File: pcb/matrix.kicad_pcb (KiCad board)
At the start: 2 copper layers, 57.4 x 47.1 mm, 69 parts, among them J1 Conn_01x02, J2 USB_C_Receptacle_USB2.0_14P, SW1 SW_Push, SW2 SW_Push, SW3 SW_Push, SW4 SW_Push, U1 ESP32-S3-MINI-1U, U2 XC6206PxxxMR

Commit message: Replace components
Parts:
- removed SW4: SW_Push, Button_Switch_SMD:SW_SPST_PTS810
- added G***: LOGO, LOGO, F.Cu at (122.6, 85.0)
- added REF**: ToolingHole_1.152mm, MountingHole:ToolingHole_1.152mm, F.Cu at (116.8, 79.0)
- added REF**: ToolingHole_1.152mm, MountingHole:ToolingHole_1.152mm, F.Cu at (116.8, 122.6)
- added REF**: ToolingHole_1.152mm, MountingHole:ToolingHole_1.152mm, F.Cu at (169.6, 122.6)
- SW1, SW2, SW3: footprint Button_Switch_SMD:SW_SPST_PTS810 -> Button_Switch_SMD:SW_SPST_TS-1088-xR020
- U1: value ESP32-S3-MINI-1U -> ESP32-C3-WROOM-02; footprint RF_Module:ESP32-S2-MINI-1U -> RF_Module:ESP32-C3-WROOM-02
- moved R3 26.0 mm to (143.0, 89.8)
- moved C3 26.0 mm to (143.0, 91.5), turned to 180 degrees
- moved R4 25.0 mm to (169.8, 86.6), turned to -90 degrees
- moved SW3 8.06 mm to (130.7, 85.1)
- moved U1 3.65 mm to (158.6, 91.6)
- moved C5 2.57 mm to (143.0, 85.8)
- moved C4 2.44 mm to (143.0, 87.6)
- moved C1 1.94 mm to (156.2, 118.2)
- moved C2 1.94 mm to (148.6, 118.2)
- moved J1 1.94 mm to (164.5, 118.3)
- moved J2 1.94 mm to (164.2, 104.7)
- moved R11 1.94 mm to (154.9, 102.9)
- moved R12 1.94 mm to (154.9, 100.4)
- moved D31 1.94 mm to (152.2, 111.8)
- moved D32 1.94 mm to (152.2, 113.8)
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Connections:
- R10 pad 1: Net-(U1-IO4) -> /P6
- R11 pad 2: Net-(U1-USB_D-) -> /USB-
- R12 pad 2: Net-(U1-USB_D+) -> /USB+
- R5 pad 1: Net-(U1-IO9) -> /P1
- R6 pad 1: Net-(U1-IO8) -> /P2
- R7 pad 1: Net-(U1-IO7) -> /P3
- R8 pad 1: Net-(U1-IO6) -> /P4
- R9 pad 1: Net-(U1-IO5) -> /P5
- U1 pad 1: GND -> Net-(U1-3V3)
- U1 pad 10: Net-(U1-IO6) -> Net-(U1-IO10)
- U1 pad 11: Net-(U1-IO7) -> unconnected-(U1-IO20/RXD-Pad11)
- U1 pad 12: Net-(U1-IO8) -> unconnected-(U1-IO21/TXD-Pad12)
- U1 pad 13: Net-(U1-IO9) -> /USB-
- U1 pad 14: Net-(U1-IO10) -> /USB+
- U1 pad 15: Net-(U1-IO11) -> /P5
- U1 pad 17: unconnected-(U1-IO13-Pad17) -> /P6
- U1 pad 18: unconnected-(U1-IO14-Pad18) -> Net-(U1-IO0)
- U1 pad 19: unconnected-(U1-IO15-Pad19) -> GND
- U1 pad 2: GND -> Net-(U1-EN)
- U1 pad 3: Net-(U1-3V3) -> /P4
- U1 pad 4: Net-(U1-IO0) -> /P3
- U1 pad 5: unconnected-(U1-IO1-Pad5) -> /P2
- U1 pad 6: unconnected-(U1-IO2-Pad6) -> /P1
- U1 pad 8: Net-(U1-IO4) -> unconnected-(U1-IO9-Pad8)
- U1 pad 9: Net-(U1-IO5) -> GND
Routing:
- net /P6: track 0.00 -> 38.2 mm, vias 0 -> 2
- net /P5: track 0.00 -> 38.0 mm, vias 0 -> 2
- net Net-(U1-IO9): track 27.2 -> 0.00 mm
- net /P1: track 0.00 -> 26.7 mm
- net /P2: track 0.00 -> 25.2 mm
- net Net-(U1-IO8): track 25.0 -> 0.00 mm
- net Net-(U1-IO11): track 24.6 -> 0.00 mm, vias 2 -> 0
- net /P3: track 0.00 -> 23.7 mm
- net Net-(U1-IO7): track 23.0 -> 0.00 mm
- net Net-(U1-3V3): track 68.7 -> 91.4 mm, vias 6 -> 2
- net /P4: track 0.00 -> 22.0 mm
- net Net-(U1-EN): track 63.9 -> 42.1 mm
- net Net-(U1-IO6): track 21.2 -> 0.00 mm
- net Net-(U1-IO5): track 18.9 -> 0.00 mm
- net /USB-: track 0.00 -> 17.3 mm
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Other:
- board size 57.4 x 47.1 mm -> 56.4 x 47.1 mm

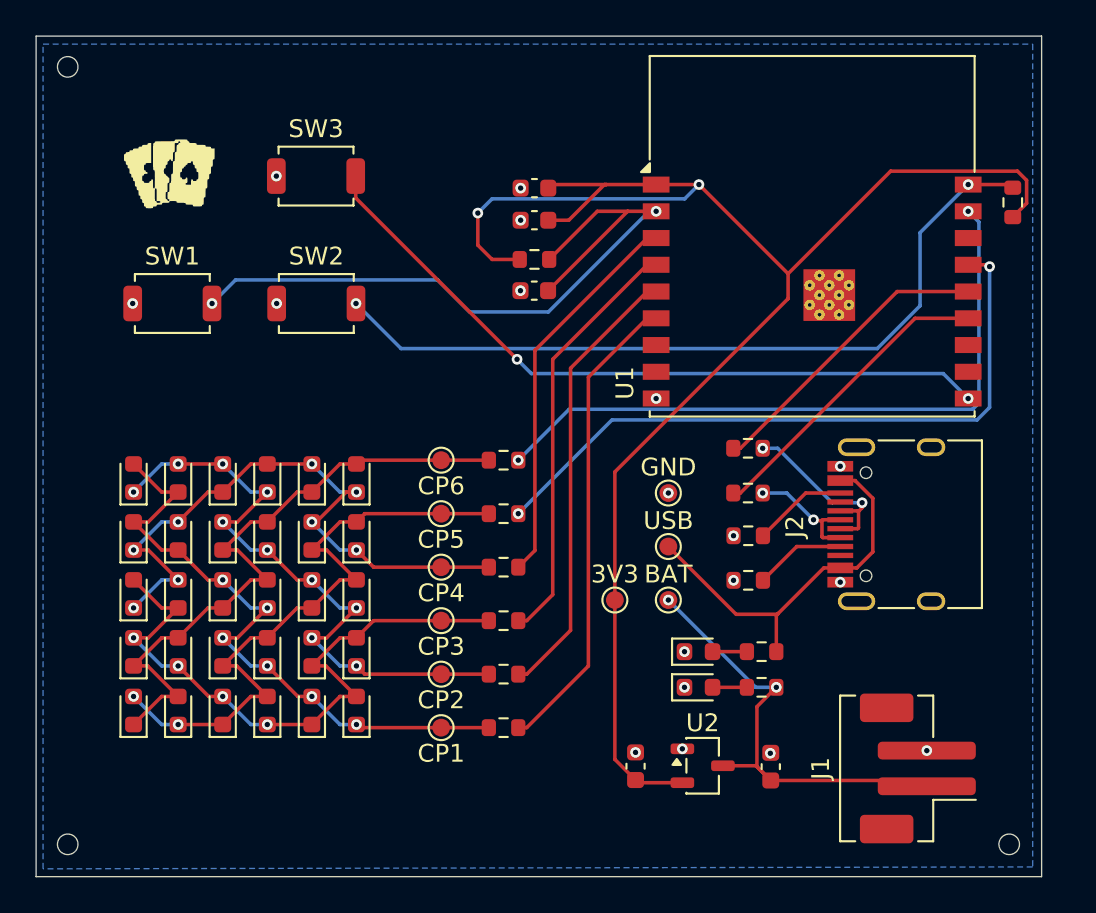
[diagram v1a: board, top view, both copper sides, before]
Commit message: Update to C6-MINI
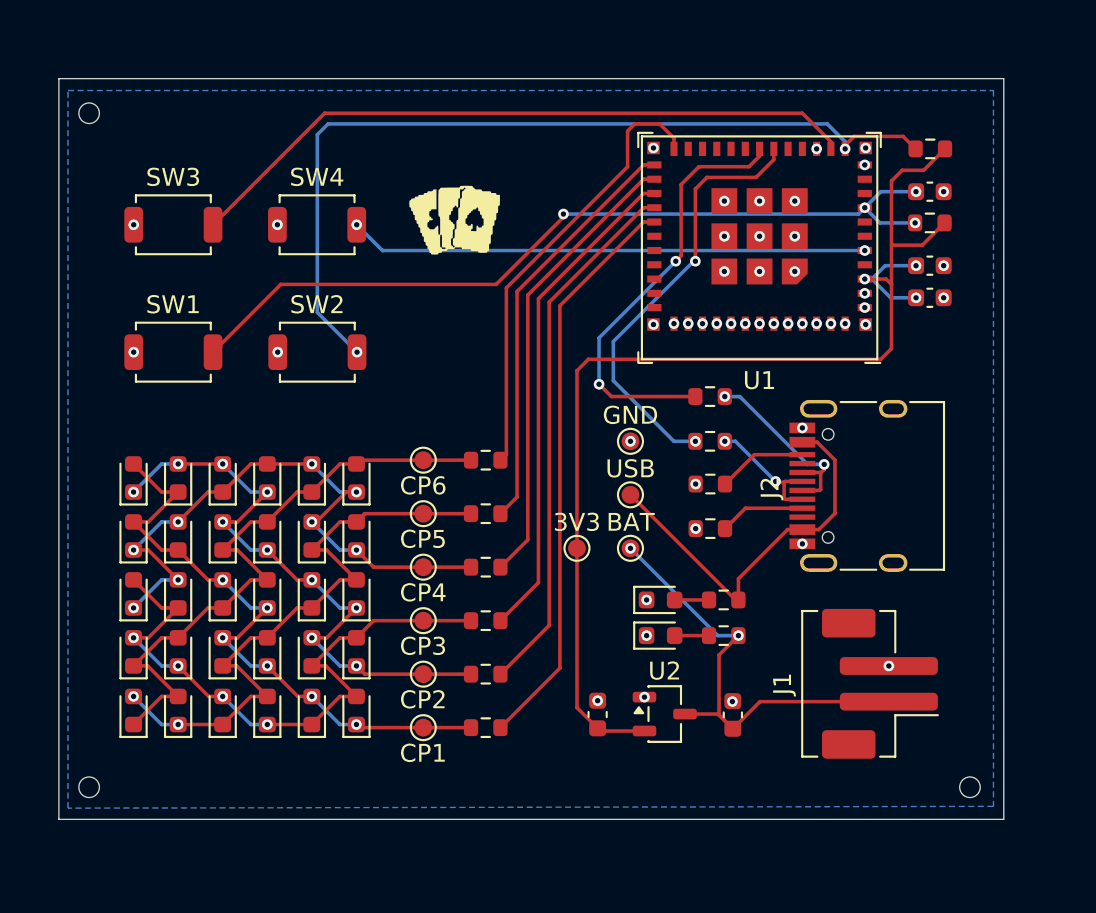
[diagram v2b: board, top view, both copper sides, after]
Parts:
- added SW4: SW_Push, Button_Switch_SMD:SW_SPST_TS-1088-xR020, F.Cu at (130.8, 87.9)
- U1: value ESP32-C3-WROOM-02 -> ESP32-C6-MINI-1/U; footprint RF_Module:ESP32-C3-WROOM-02 -> PCM_Espressif:ESP32-C6-MINI-1U
- moved C3 22.9 mm to (165.2, 86.0), turned to 0 degrees
- moved C4 22.6 mm to (165.2, 92.0)
- moved C5 22.6 mm to (165.2, 90.2)
- moved R3 22.3 mm to (165.2, 87.8), turned to 0 degrees
- moved G*** 16.2 mm to (138.6, 87.6)
- moved SW3 8.45 mm to (122.7, 87.9)
- moved R4 5.51 mm to (165.2, 83.6), turned to 0 degrees
- moved J1 5.20 mm to (162.3, 113.6)
- moved REF** 3.88 mm to (167.4, 119.4)
- moved 3V3 3.60 mm to (145.4, 106.0)
- moved BAT 3.60 mm to (148.4, 106.0)
- moved C1 3.60 mm to (154.1, 115.3)
- moved C2 3.60 mm to (146.5, 115.3)
- moved GND 3.60 mm to (148.4, 100.0)
- moved R11 3.60 mm to (152.8, 100.0)
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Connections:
- net Net-(J1-Pin_1) renamed +BATT
- 3V3 pad 1: Net-(U1-3V3) -> +3V3
- C2 pad 1: Net-(U1-3V3) -> +3V3
- C3 pad 1: Net-(U1-EN) -> /EN
- C4 pad 1: GND -> +3V3
- C4 pad 2: Net-(U1-3V3) -> GND
- C5 pad 1: GND -> +3V3
- C5 pad 2: Net-(U1-3V3) -> GND
- R11 pad 2: /USB- -> /D-
- R12 pad 2: /USB+ -> /D+
- R3 pad 1: Net-(U1-EN) -> /EN
- R3 pad 2: Net-(U1-3V3) -> +3V3
- R4 pad 1: Net-(U1-IO0) -> /GP0
- R4 pad 2: Net-(U1-3V3) -> +3V3
- SW1 pad 2: Net-(U1-EN) -> /EN
- SW2 pad 2: Net-(U1-IO0) -> /GP0
- SW3 pad 2: Net-(U1-IO10) -> /GP1
- U1 pad 1: Net-(U1-3V3) -> GND
- U1 pad 10: Net-(U1-IO10) -> unconnected-(U1-MTDI/GPIO5/ADC1_CH5-Pad10)
- U1 pad 11: unconnected-(U1-IO20/RXD-Pad11) -> GND
- U1 pad 12: unconnected-(U1-IO21/TXD-Pad12) -> /GP0
- U1 pad 13: /USB- -> /GP1
- U1 pad 14: /USB+ -> GND
- U1 pad 15: /P5 -> unconnected-(U1-MTCK/GPIO6/ADC1_CH6-Pad15)
- U1 pad 17: /P6 -> /D-
- U1 pad 18: Net-(U1-IO0) -> /D+
- U1 pad 19: GND -> unconnected-(U1-GPIO14-Pad19)
- U1 pad 2: Net-(U1-EN) -> GND
- U1 pad 3: /P4 -> +3V3
- U1 pad 4: /P3 -> unconnected-(U1-NC-Pad4)
- U1 pad 5: /P2 -> /GP2
- U1 pad 6: /P1 -> unconnected-(U1-GPIO3/ADC1_CH3-Pad6)
- U1 pad 8: unconnected-(U1-IO9-Pad8) -> /EN
- U1 pad 9: GND -> unconnected-(U1-MTMS/GPIO4/ADC1_CH4-Pad9)
- U2 pad 2: Net-(U1-3V3) -> +3V3
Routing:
- net Net-(U1-3V3): track 91.4 -> 0.00 mm, vias 2 -> 0
- net +3V3: track 0.00 -> 66.0 mm, vias 0 -> 3
- net /GP0: track 0.00 -> 48.4 mm, vias 0 -> 2
- net /EN: track 0.00 -> 46.4 mm, vias 0 -> 4
- net Net-(U1-IO0): track 44.2 -> 0.00 mm, vias 2 -> 0
- net Net-(U1-EN): track 42.1 -> 0.00 mm, vias 2 -> 0
- net Net-(U1-IO10): track 40.2 -> 0.00 mm, vias 2 -> 0
- net /GP1: track 0.00 -> 38.3 mm
- net /GP2: track 0.00 -> 29.1 mm, vias 0 -> 2
- net /D-: track 0.00 -> 24.5 mm, vias 0 -> 2
- net /D+: track 0.00 -> 24.4 mm, vias 0 -> 2
- net /USB-: track 17.3 -> 0.00 mm
- net /USB+: track 16.9 -> 0.00 mm
- net /P5: track 38.0 -> 23.5 mm, vias 2 -> 0
- net /P6: track 38.2 -> 25.1 mm, vias 2 -> 0
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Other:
- board size 56.4 x 47.1 mm -> 53 x 41.5 mm
